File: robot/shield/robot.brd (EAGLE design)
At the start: 69.5 x 53.3 mm, 18 parts, among them IC1 LM386N-1, M2 ARDUINO_R3_ICSP, X1 22-23-2021, X2 22-23-2021, X3 22-23-2031, X4 22-23-2031, X5 22-23-2051

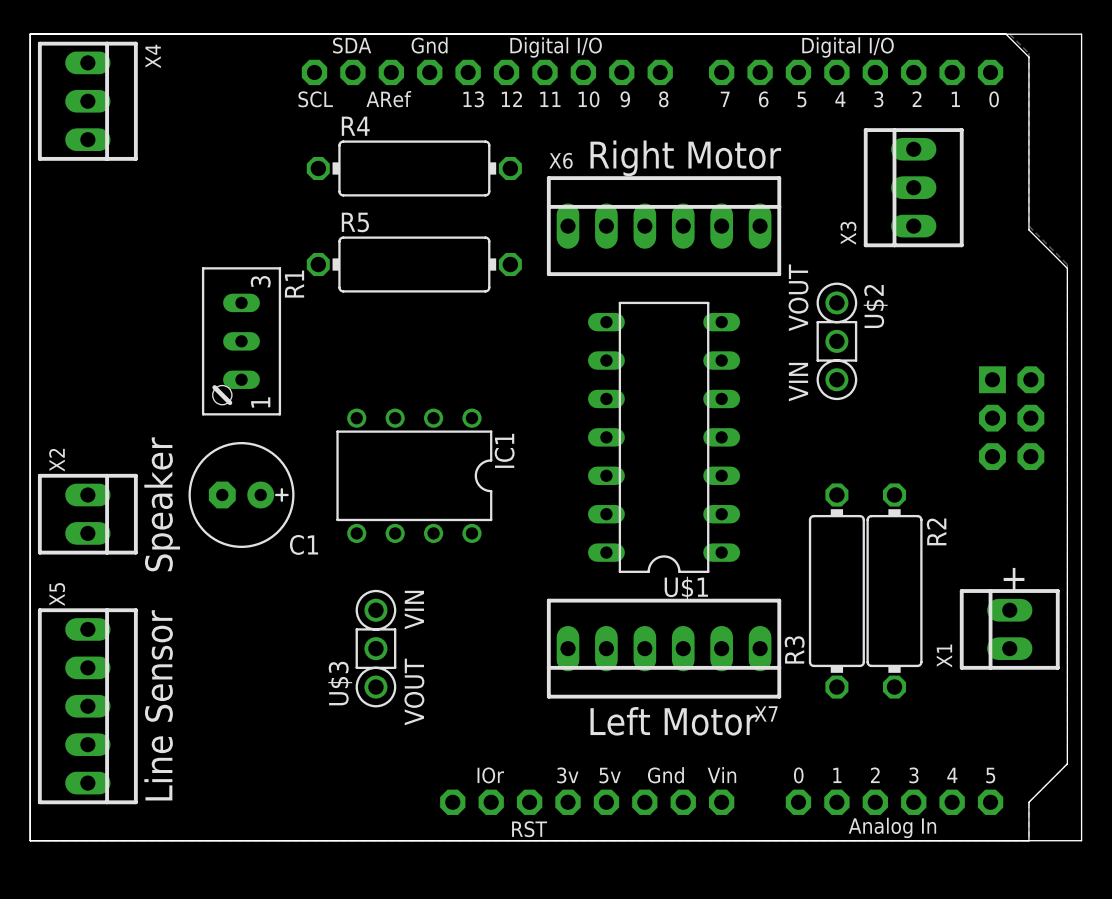
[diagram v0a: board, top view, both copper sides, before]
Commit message: Update pin assignments; layout
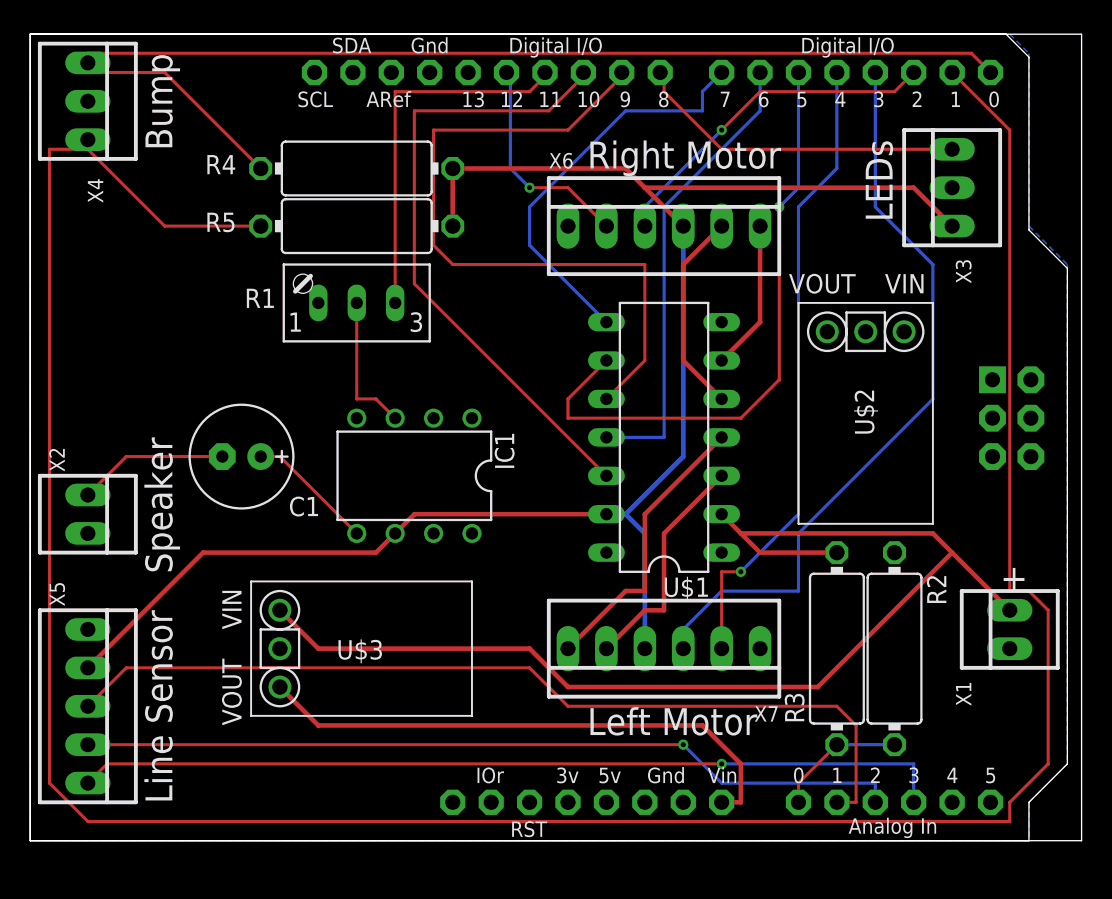
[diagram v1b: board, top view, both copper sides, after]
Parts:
- moved R1 9.67 mm to (21.6, 36.8), turned to 180 degrees
- moved U$3 6.35 mm to (16.5, 12.7)
- moved R5 4.58 mm to (21.6, 40.6)
- moved R2 3.81 mm to (57.1, 12.7)
- moved R3 3.81 mm to (53.3, 12.7)
- moved R4 3.81 mm to (21.6, 44.5)
- moved C1 2.54 mm to (14.0, 25.4)
- moved X3 2.54 mm to (61.0, 43.2)
- moved U$2 2.01 mm to (55.2, 33.7), turned to 0 degrees
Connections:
- net AENABLE: now also M2.D9; no longer M2.D5
- net APHASE: now also M2.D5; no longer M2.D7
- net AUDIO: now also M2.D11; no longer M2.D4
- net BENABLE: now also M2.D10; no longer M2.D6
- net BPHASE: now also M2.D6; no longer M2.D11
- net DRV8835_MODE: now also M2.D7; no longer M2.D3
- net LEDS: now also M2.D8; no longer M2.D2
- net LENCODER_A: now also M2.D3; no longer M2.D8
- net LENCODER_B: now also M2.D4; no longer M2.D9
- net RENCODER_A: now also M2.D2; no longer M2.D10
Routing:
- net RBUMP: track 0.00 -> 177.1 mm
- net +5V: track 0.00 -> 111.8 mm
- net VBAT: track 0.00 -> 78.8 mm
- net LBUMP: track 0.00 -> 75.5 mm
- net LINE1: track 0.00 -> 59.8 mm
- net LINE3: track 0.00 -> 57.7 mm, vias 0 -> 1
- net LINE2: track 0.00 -> 54.4 mm, vias 0 -> 1
- net LENCODER_A: track 0.00 -> 49.5 mm
- net AENABLE: track 0.00 -> 46.6 mm
- net BENABLE: track 0.00 -> 42.1 mm
- net LENCODER_B: track 0.00 -> 42.0 mm, vias 0 -> 1
- net APHASE: track 0.00 -> 40.7 mm, vias 0 -> 1
- net N$5: track 0.00 -> 36.4 mm
- net BPHASE: track 0.00 -> 30.6 mm
- net DRV8835_MODE: track 0.00 -> 26.9 mm
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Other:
- board text added: "Bump"
- board text added: "LEDs"

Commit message: Updates to schematic and layout
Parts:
- removed R4, R5: 10K, adafruit:V234/12
- moved X4 58.6 mm to (62.2, 43.8), turned to 90 degrees
- moved X3 57.4 mm to (3.81, 48.3), turned to 270 degrees
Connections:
- net +5V: no longer R4.2, R5.2
- net BATLEVEL: now also M2.A3; no longer M2.A0
- net LBUMP: no longer R4.1
- net LINE1: now also M2.A0; no longer M2.A1
- net LINE2: now also M2.A1; no longer M2.A2
- net LINE3: now also M2.A2; no longer M2.A3
- net RBUMP: no longer R5.1
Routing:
- net RBUMP: track 177.1 -> 4.97 mm
- net LBUMP: track 75.5 -> 10.5 mm
- net AENABLE: track 46.6 -> 23.5 mm
- net +5V: track 111.8 -> 134.0 mm
- net LEDS: track 22.2 -> 41.6 mm
- net APHASE: track 40.7 -> 24.3 mm, vias 1 -> 0
- net LINE1: track 59.8 -> 50.6 mm
- net BPHASE: track 30.6 -> 38.8 mm
- net DRV8835_MODE: track 26.9 -> 19.7 mm
- net LINE3: track 57.7 -> 62.3 mm, vias 1 -> 0
- net BENABLE: track 42.1 -> 37.6 mm
- net RENCODER_A: track 22.7 -> 27.1 mm, vias 1 -> 0
- net N$5: track 36.4 -> 32.4 mm
- net VBAT: track 78.8 -> 75.7 mm
- net AUDIO: track 24.9 -> 22.7 mm
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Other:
- board text added: "5 V"
- board text added: "9 V"
- board text added: "CoderDojoBot Rev 1"

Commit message: Board version that was sent to OSH Park
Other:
- board size 69.5 x 53.3 mm -> 68.6 x 53.3 mm
- board text added: "5V"
- board text added: "9V"
- board text added: "Line"
- board text removed: "5 V"
- board text removed: "9 V"
- board text removed: "Line Sensor"
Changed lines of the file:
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@@
 <board>
 <plain>
-<wire x1="0" y1="0" x2="69.52" y2="0" width="0" layer="20"/>
-<wire x1="69.52" y1="0" x2="69.52" y2="53.33" width="0" layer="20"/>
-<wire x1="69.52" y1="53.33" x2="0" y2="53.33" width="0" layer="20"/>
-<wire x1="0" y1="53.33" x2="0" y2="0" width="0" layer="20"/>
 <text x="64.135" y="16.51" size="1.778" layer="21">+</text>
-<text x="7.62" y="15.24" size="1.778" layer="21" rot="R270">Line Sensor</text>
+<text x="7.62" y="11.43" size="1.778" layer="21" font="vector" rot="R270">Line</text>
 <text x="7.62" y="26.67" size="1.778" layer="21" rot="R270">Speaker</text>
-<text x="36.83" y="44.45" size="1.778" layer="21">Right Motor</text>
-<text x="36.83" y="6.985" size="1.778" layer="21">Left Motor</text>
+<text x="35.56" y="44.45" size="1.778" layer="21">Right Motor</text>
+<text x="34.925" y="6.985" size="1.778" layer="21">Left Motor</text>
 <text x="56.515" y="46.99" size="1.778" layer="21" rot="R270">Bump</text>
 <text x="9.525" y="45.72" size="1.778" layer="21" rot="R90">LEDs</text>
@@
 <hole x="66.04" y="35.56" drill="3.2"/>
 <hole x="66.04" y="7.62" drill="3.2"/>
-<text x="6.35" y="27.305" size="1.778" layer="21" rot="R90">CoderDojoBot
+<text x="5.715" y="25.4" size="1.778" layer="21" rot="R90">CoderDojoBot
 Rev 1</text>
-<text x="19.05" y="12.065" size="1.778" layer="21">9 V</text>
-<text x="56.515" y="27.305" size="1.778" layer="21" rot="R90">5 V</text>
+<text x="20.32" y="12.065" size="1.778" layer="21">9V</text>
+<text x="56.515" y="24.765" size="1.778" layer="21" rot="R90">5V</text>
 </plain>
 <attributes>
@@
 </autorouter>
 <elements>
-<element name="IC1" library="linear" package="DIL08" value="LM386N-1" x="25.4" y="24.13" rot="R180"/>
-<element name="U$1" library="robot" package="DIL14" value="DRV8835" x="41.91" y="26.67" rot="R90"/>
+<element name="IC1" library="linear" package="DIL08" value="LM386N-1" x="25.4" y="24.13" smashed="yes" rot="R180">
+<attribute name="NAME" x="30.734" y="27.051" size="1.27" layer="25" ratio="10" rot="R270"/>
+<attribute name="VALUE" x="28.956" y="24.765" size="1.016" layer="27" font="vector" ratio="10" rot="R180"/>
+</element>
+<element name="U$1" library="robot" package="DIL14" value="DRV8835" x="41.91" y="26.67" smashed="yes" rot="R90">
+<attribute name="VALUE" x="42.545" y="22.479" size="1.27" layer="27" ratio="10" rot="R90"/>
+</element>
 <element name="C1" library="adafruit" package="E2,5-7" value="220" x="13.97" y="25.4" smashed="yes" rot="R180">
 <attribute name="NAME" x="19.177" y="22.733" size="1.27" layer="25" ratio="10" rot="R180"/>
@@
 </element>
 <element name="U$2" library="robot" package="POLOLU-REG" value="S7V7F5" x="55.245" y="33.655" smashed="yes"/>
-<element name="R2" library="adafruit" package="V234/12" value="10K" x="57.15" y="12.7" rot="R270"/>
+<element name="R2" library="adafruit" package="V234/12" value="10K" x="57.15" y="12.7" smashed="yes" rot="R270">
+<attribute name="NAME" x="59.309" y="10.033" size="1.27" layer="25" ratio="10" rot="R270"/>
+<attribute name="VALUE" x="56.515" y="12.7" size="1.27" layer="27" ratio="10" rot="R270"/>
+</element>
 <element name="R3" library="adafruit" package="V234/12" value="10K" x="53.34" y="12.7" rot="R90"/>
 <element name="U$3" library="robot" package="POLOLU-REG" value="U3V12F9" x="16.51" y="12.7" smashed="yes" rot="R90"/>
@@
 <attribute name="MF" value="MOLEX" x="64.77" y="13.97" size="1.778" layer="27" rot="R90" display="off"/>
 <attribute name="OC_FARNELL" value="1462926" x="64.77" y="13.97" size="1.778" layer="27" rot="R90" display="off"/>
-<attribute name="NAME" x="62.23" y="8.89" size="1.016" layer="25" ratio="10" rot="R90"/>
+<attribute name="NAME" x="62.23" y="9.525" size="1.016" layer="25" ratio="10" rot="R90"/>
 </element>
 <element name="X2" library="con-molex" package="22-23-2021" value="22-23-2021" x="3.81" y="21.59" smashed="yes" rot="R270">
@@
 <attribute name="NAME" x="1.27" y="17.145" size="1.016" layer="25" ratio="10" rot="R270"/>
 </element>
-<element name="X6" library="con-molex" package="22-23-2061" value="" x="41.91" y="40.64">
+<element name="X6" library="con-molex" package="22-23-2061" value="" x="41.91" y="40.64" smashed="yes">
 <attribute name="OC_NEWARK" value="27C1933" x="41.91" y="40.64" size="1.778" layer="27" display="off"/>
 <attribute name="MPN" value="22-23-2061" x="41.91" y="40.64" size="1.778" layer="27" display="off"/>
 <attribute name="MF" value="MOLEX" x="41.91" y="40.64" size="1.778" layer="27" display="off"/>
 <attribute name="OC_FARNELL" value="1462922" x="41.91" y="40.64" size="1.778" layer="27" display="off"/>
-</element>
-<element name="X7" library="con-molex" package="22-23-2061" value="" x="41.91" y="12.7" rot="R180">
+<attribute name="NAME" x="33.02" y="35.56" size="1.016" layer="25" ratio="10"/>
+<attribute name="VALUE" x="34.29" y="35.56" size="1.016" layer="27" ratio="10"/>
+</element>
+<element name="X7" library="con-molex" package="22-23-2061" value="" x="41.91" y="12.7" smashed="yes" rot="R180">
 <attribute name="OC_NEWARK" value="27C1933" x="41.91" y="12.7" size="1.778" layer="27" rot="R180" display="off"/>
 <attribute name="MPN" value="22-23-2061" x="41.91" y="12.7" size="1.778" layer="27" rot="R180" display="off"/>
 <attribute name="MF" value="MOLEX" x="41.91" y="12.7" size="1.778" layer="27" rot="R180" display="off"/>
 <attribute name="OC_FARNELL" value="1462922" x="41.91" y="12.7" size="1.778" layer="27" rot="R180" display="off"/>
+<attribute name="NAME" x="34.29" y="16.51" size="1.016" layer="25" ratio="10" rot="R180"/>
+<attribute name="VALUE" x="49.53" y="17.78" size="1.016" layer="27" ratio="10" rot="R180"/>
 </element>
 </elements>
